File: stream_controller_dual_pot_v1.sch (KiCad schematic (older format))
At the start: 35 parts, among them Q1 Q_PMOS_GDS, Q2 Q_PMOS_GDS, SW1 SW_SPDT, U1 MCP1825S, U2 MCP2221AxSL, U3 MCP73831-2-OT, U5 ESP32_WROVER_E, U6 MIC803

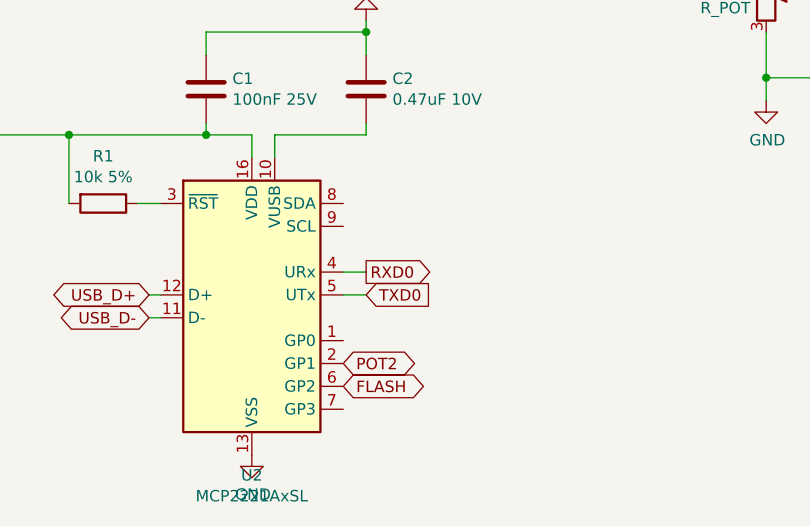
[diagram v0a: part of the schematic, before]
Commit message: bug UART corrigé
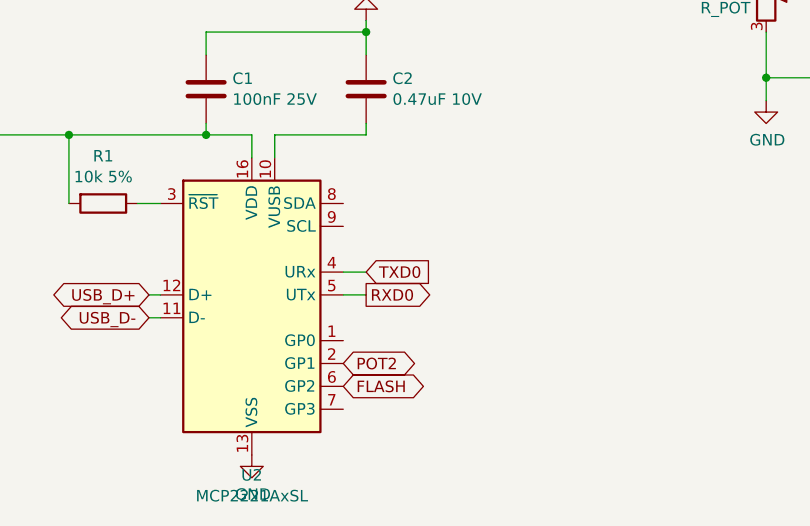
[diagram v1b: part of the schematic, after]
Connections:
- net RXD0: now also U2.5 (UTx); no longer U2.4 (URx)
- net TXD0: now also U2.4 (URx); no longer U2.5 (UTx)
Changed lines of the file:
@@
 Text GLabel 3400 4900 0    50   BiDi ~ 0
 USB_D-
-Text GLabel 4350 4700 2    50   Output ~ 0
+Text GLabel 4350 4800 2    50   Output ~ 0
 RXD0
-Text GLabel 4350 4800 2    50   Input ~ 0
+Text GLabel 4350 4700 2    50   Input ~ 0
 TXD0
 Text GLabel 9200 3900 2    50   Input ~ 0

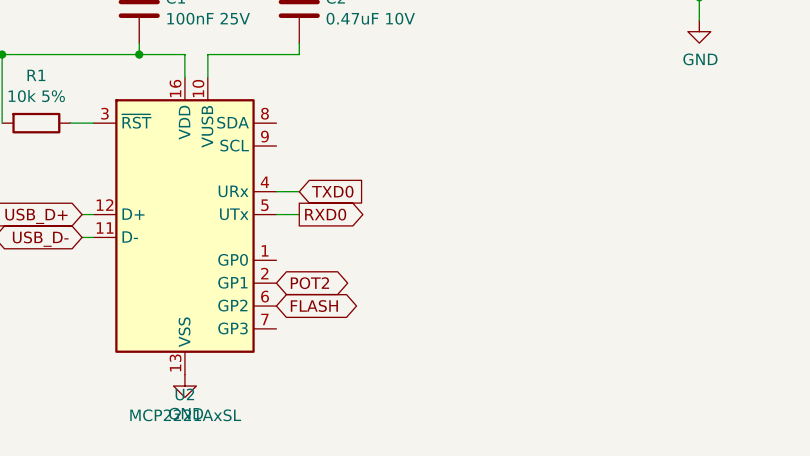
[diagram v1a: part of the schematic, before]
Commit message: Correction IO0 forcé à 1
Si IO0 n'est pas haut au démarrage, l'ESP32 se met en mode flash. Quand non-connecté par USB, IO0 doit être forcé à 1, car le contrôleur USB n'est pas alimenté.
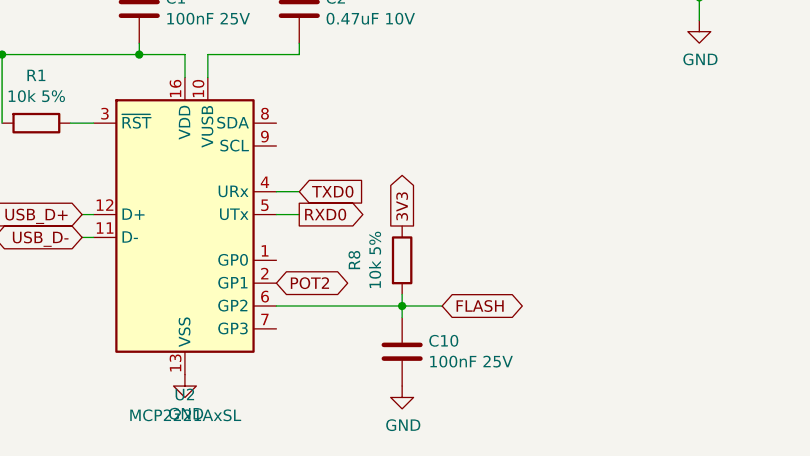
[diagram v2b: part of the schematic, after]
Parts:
- added C10: 100nF 25V, Capacitor_SMD:C_0402_1005Metric_Pad0.74x0.62mm_HandSolder, symbol Device:C
- added R8: 10k 5%, Resistor_SMD:R_0402_1005Metric_Pad0.72x0.64mm_HandSolder, symbol Device:R
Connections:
- net 3V3: now also R8.1
- net FLASH: now also C10.1, R8.2
- net GND: now also C10.2
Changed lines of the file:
@@
 EndData
 $EndBitmap
-Text GLabel 4250 5200 2    50   BiDi ~ 0
+Text GLabel 4975 5200 2    50   BiDi ~ 0
 FLASH
 Text GLabel 4250 5100 2    50   BiDi ~ 0
@@
 	3750 3300 3750 2250
 $Comp
-L power:GND #PWR?
+L power:GND #PWR0113
 U 1 1 6090601E
 P 3850 5500
-F 0 "#PWR?" H 3850 5250 50  0001 C CNN
+F 0 "#PWR0113" H 3850 5250 50  0001 C CNN
 F 1 "GND" H 3855 5327 50  0000 C CNN
 F 2 "" H 3850 5500 50  0001 C CNN
@@
 	1    0    0    -1
 $EndComp
+$Comp
+L Device:R R8
+U 1 1 609456D2
+P 4800 5000
+F 0 "R8" V 4593 5000 50  0000 C CNN
+F 1 "10k 5%" V 4684 5000 50  0000 C CNN
+F 2 "Resistor_SMD:R_0402_1005Metric_Pad0.72x0.64mm_HandSolder" V 4730 5000 50  0001 C CNN
+F 3 "~" H 4800 5000 50  0001 C CNN
+	1    4800 5000
+	1    0    0    -1
+$EndComp
+Wire Wire Line
+	4800 5150 4800 5200
+Wire Wire Line
+	4800 5200 4250 5200
+Text GLabel 4800 4850 1    50   Output ~ 0
+3V3
+$Comp
+L Device:C C10
+U 1 1 60958AC1
+P 4800 5400
+F 0 "C10" H 4915 5446 50  0000 L CNN
+F 1 "100nF 25V" H 4915 5355 50  0000 L CNN
+F 2 "Capacitor_SMD:C_0402_1005Metric_Pad0.74x0.62mm_HandSolder" H 4838 5250 50  0001 C CNN
+F 3 "~" H 4800 5400 50  0001 C CNN
+	1    4800 5400
+	1    0    0    -1
+$EndComp
+Wire Wire Line
+	4975 5200 4800 5200
+Connection ~ 4800 5200
+$Comp
+L power:GND #PWR0118
+U 1 1 60972D20
+P 4800 5550
+F 0 "#PWR0118" H 4800 5300 50  0001 C CNN
+F 1 "GND" H 4805 5377 50  0000 C CNN
+F 2 "" H 4800 5550 50  0001 C CNN
+F 3 "" H 4800 5550 50  0001 C CNN
+	1    4800 5550
+	1    0    0    -1
+$EndComp
+Wire Wire Line
+	4800 5200 4800 5250
 $EndSCHEMATC

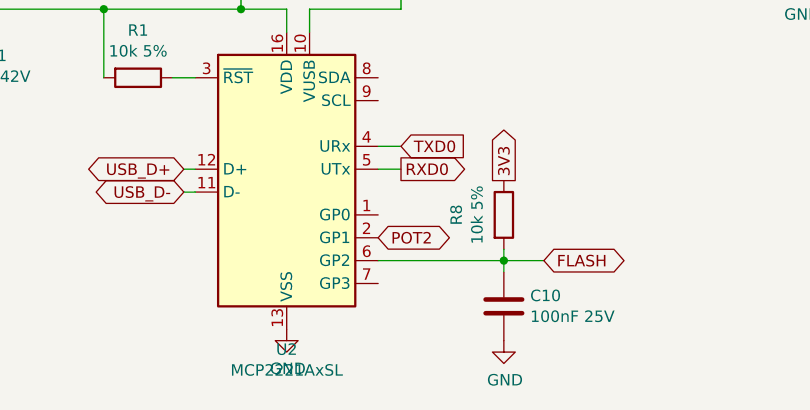
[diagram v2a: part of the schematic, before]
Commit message: Ajout contrôle pin EN par contrôleur USB
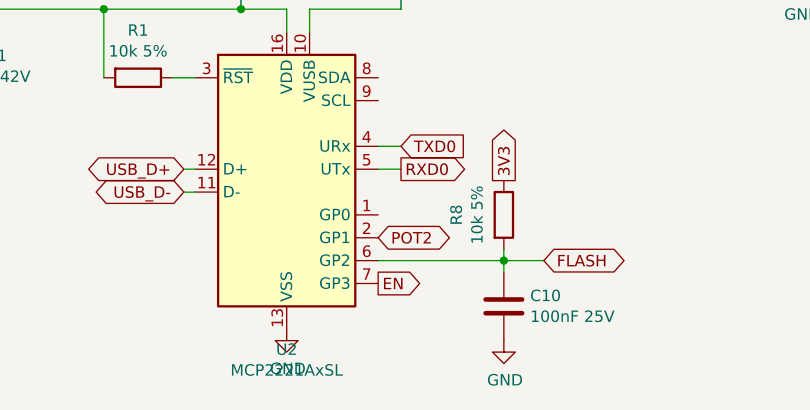
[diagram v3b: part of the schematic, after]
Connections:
- net EN: now also U2.7 (GP3)
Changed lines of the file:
@@
 Wire Wire Line
 	4800 5200 4800 5250
+Text GLabel 4250 5300 2    50   Output ~ 0
+EN
 $EndSCHEMATC

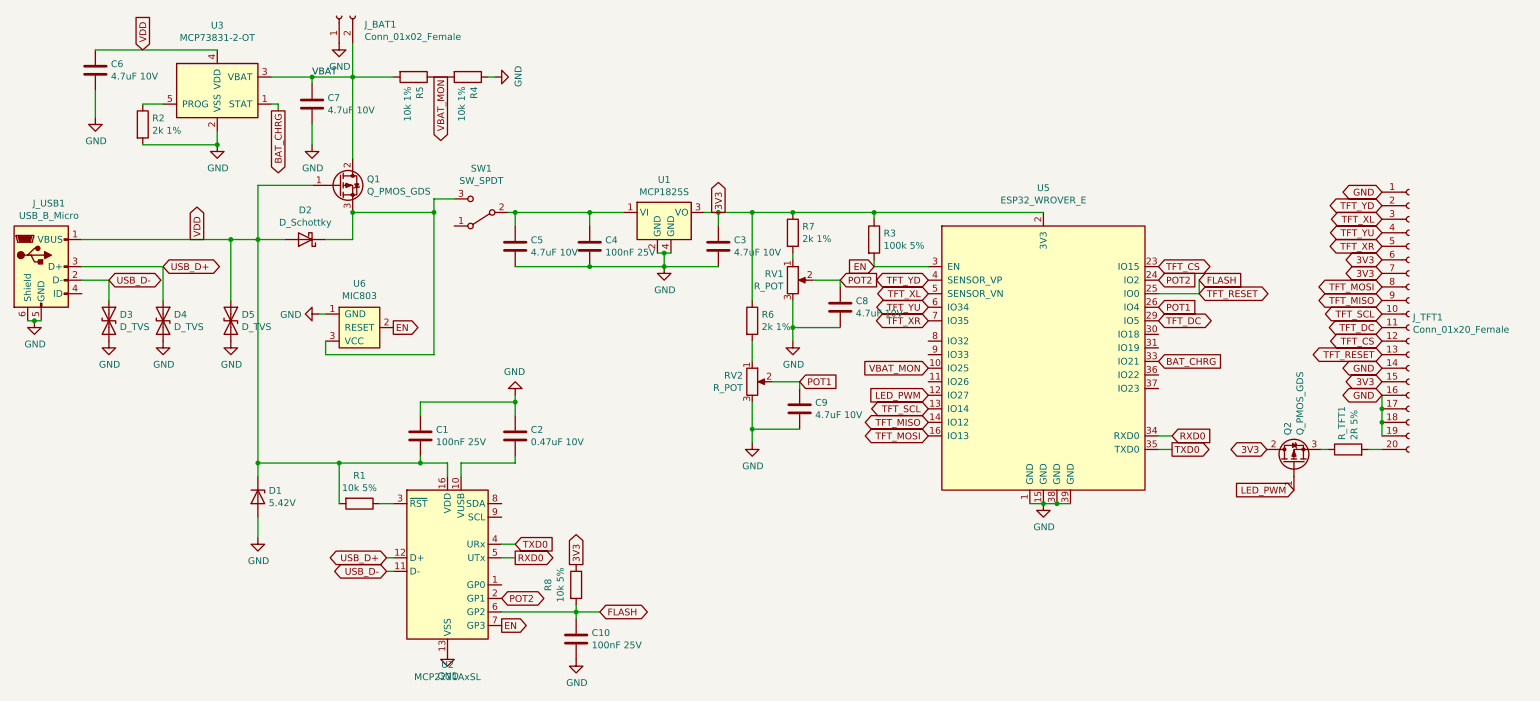
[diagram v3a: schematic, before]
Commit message: Changements divers
Modifications :
 - toutes les entrées analogiques sur ADC1, car ADC2 ne peut pas être utilisé si le WiFi est actif
 - lecture de l'écran tactile déplacée sur pattes 8, 9, 10 et 11, car les pattes 4, 5, 6 et 7 sont en lecture seule
 - changement du transistor pour le contrôle de la luminosité de l'écran
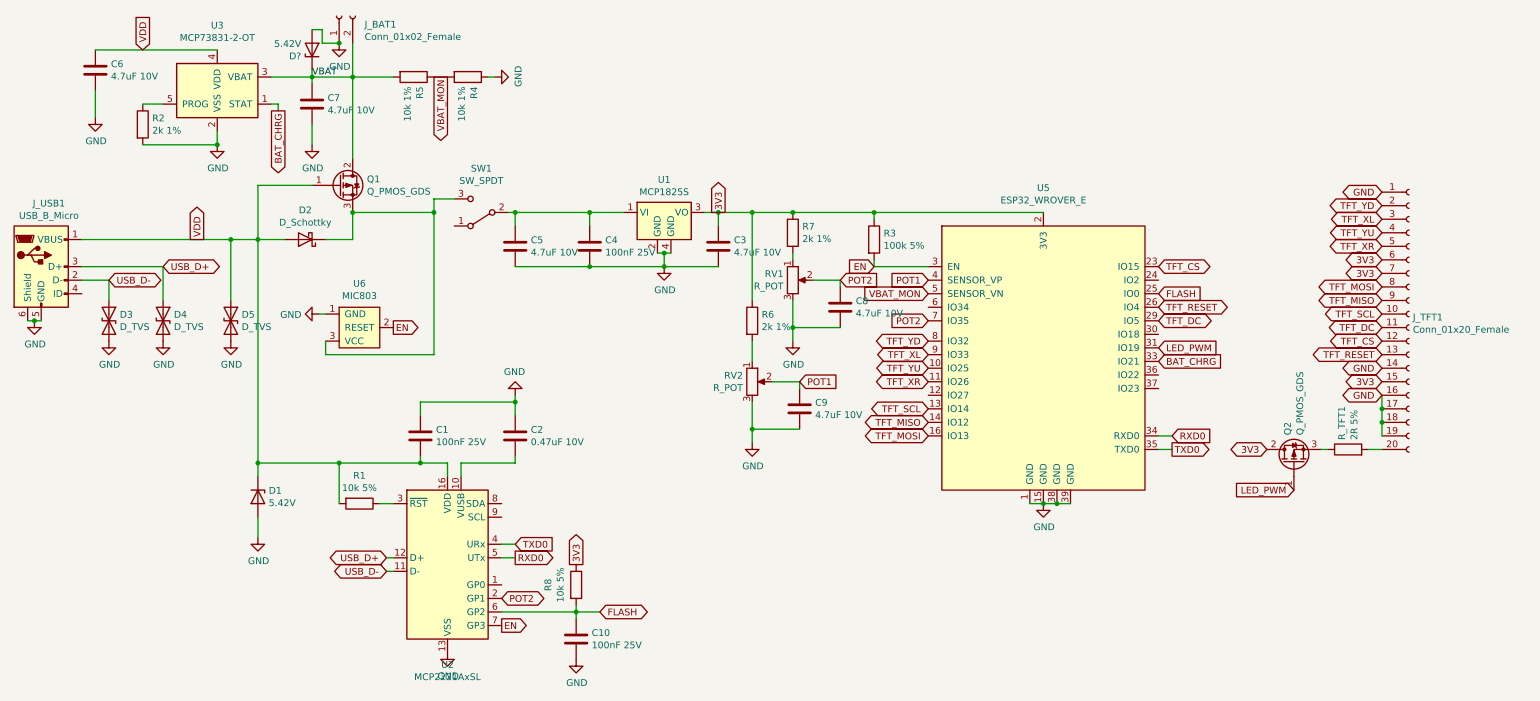
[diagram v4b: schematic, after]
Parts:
- added D?: 5.42V, Diode_SMD:D_SOD-323F, symbol Device:D_Zener
- J_BAT1: footprint Connector_PinHeader_2.54mm:PinHeader_1x02_P2.54mm_Vertical -> misc_vp:CLM-101-02-L-D
- Q2: footprint Package_DFN_QFN:Diodes_DFN1006-3 -> Package_TO_SOT_SMD:SOT-23
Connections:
- net FLASH: no longer J_TFT1.13 (Pin_13)
- net GND: now also D?.2 (A)
- net LED_PWM: now also U5.31 (IO19); no longer U5.12 (IO27)
- net POT1: now also U5.4 (SENSOR_VP); no longer U5.26 (IO4)
- net POT2: now also U5.7 (IO35); no longer U5.24 (IO2)
- net TFT_XL: now also U5.9 (IO33); no longer U5.5 (SENSOR_VN)
- net TFT_XR: now also U5.11 (IO26); no longer U5.7 (IO35)
- net TFT_YD: now also U5.8 (IO32); no longer U5.4 (SENSOR_VP)
- net TFT_YU: now also U5.10 (IO25); no longer U5.6 (IO34)
- net VBAT: now also D?.1 (K)
- net VBAT_MON: now also U5.5 (SENSOR_VN); no longer U5.10 (IO25)
- new net TFT_RESET: J_TFT1.13 (Pin_13), U5.26 (IO4)
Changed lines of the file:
@@
 F 0 "J_BAT1" V 2988 612 50  0000 R CNN
 F 1 "Conn_01x02_Female" V 2897 612 50  0000 R CNN
-F 2 "Connector_PinHeader_2.54mm:PinHeader_1x02_P2.54mm_Vertical" H 3050 800 50  0001 C CNN
+F 2 "misc_vp:CLM-101-02-L-D" H 3050 800 50  0001 C CNN
 F 3 "~" H 3050 800 50  0001 C CNN
 	1    3050 800
@@
 Wire Wire Line
 	4900 2250 5150 2250
-Text GLabel 7400 3400 0    50   Input ~ 0
+Text GLabel 7400 2850 0    50   Input ~ 0
 VBAT_MON
 Wire Wire Line
@@
 Text GLabel 9100 2650 2    50   BiDi ~ 0
 TFT_CS
-Text GLabel 9400 2850 2    50   BiDi ~ 0
+Text GLabel 9100 2950 2    50   BiDi ~ 0
 TFT_RESET
-Text GLabel 7400 2750 0    50   BiDi ~ 0
+Text GLabel 7400 3200 0    50   BiDi ~ 0
 TFT_YD
-Text GLabel 7400 2850 0    50   BiDi ~ 0
+Text GLabel 7400 3300 0    50   BiDi ~ 0
 TFT_XL
-Text GLabel 7400 2950 0    50   BiDi ~ 0
+Text GLabel 7400 3400 0    50   BiDi ~ 0
 TFT_YU
-Text GLabel 7400 3050 0    50   BiDi ~ 0
+Text GLabel 7400 3500 0    50   BiDi ~ 0
 TFT_XR
 Text GLabel 9100 3050 2    50   BiDi ~ 0
@@
 Text GLabel 6750 2750 2    50   Input ~ 0
 POT2
-Text GLabel 9100 2950 2    50   Input ~ 0
+Text GLabel 7400 2750 0    50   Input ~ 0
 POT1
 Text GLabel 9100 3350 2    50   Input ~ 0
@@
 Text Label 2850 1250 0    50   ~ 0
 VBAT
-Text GLabel 9100 2750 2    50   Input ~ 0
-POT2
-Text GLabel 9400 2750 2    50   Input ~ 0
+Text GLabel 9100 2850 2    50   Input ~ 0
 FLASH
 $Comp
@@
 Text GLabel 4250 5100 2    50   BiDi ~ 0
 POT2
-Wire Wire Line
-	9400 2750 9400 2850
 $Comp
 L Device:Q_PMOS_GDS Q2
@@
 F 0 "Q2" H 10305 4146 50  0000 L CNN
 F 1 "Q_PMOS_GDS" H 10305 4055 50  0000 L CNN
-F 2 "Package_DFN_QFN:Diodes_DFN1006-3" H 10300 4200 50  0001 C CNN
+F 2 "Package_TO_SOT_SMD:SOT-23" H 10300 4200 50  0001 C CNN
 F 3 "~" H 10100 4100 50  0001 C CNN
 	1    10100 4100
@@
 Text GLabel 10100 4300 0    50   Input ~ 0
 LED_PWM
-Text GLabel 7400 3600 0    50   Input ~ 0
+Text GLabel 9100 3250 2    50   Input ~ 0
 LED_PWM
-Wire Wire Line
-	9400 2850 9100 2850
 Text GLabel 3450 3100 2    50   Output ~ 0
 EN
@@
 Text GLabel 4250 5300 2    50   Output ~ 0
 EN
+Text GLabel 7400 3050 0    50   Input ~ 0
+POT2
+$Comp
+L Device:D_Zener D?
+U 1 1 609F24D1
+P 2850 1050
+F 0 "D?" V 2804 1130 50  0000 L CNN
+F 1 "5.42V" V 2895 1130 50  0000 L CNN
+F 2 "Diode_SMD:D_SOD-323F" H 2850 1050 50  0001 C CNN
+F 3 "~" H 2850 1050 50  0001 C CNN
+	1    2850 1050
+	0    -1   -1   0
+$EndComp
+Wire Wire Line
+	2850 1250 2850 1200
+Wire Wire Line
+	3050 1000 2925 1000
+Wire Wire Line
+	2925 1000 2925 900
+Wire Wire Line
+	2925 900  2850 900
+Connection ~ 3050 1000
 $EndSCHEMATC

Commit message: Corrections et ajouts
Corrigé : strapping pin 2 connectée au même signal FLASH que pin 0
Ajouté : I2C entre uC et contrôleur USB
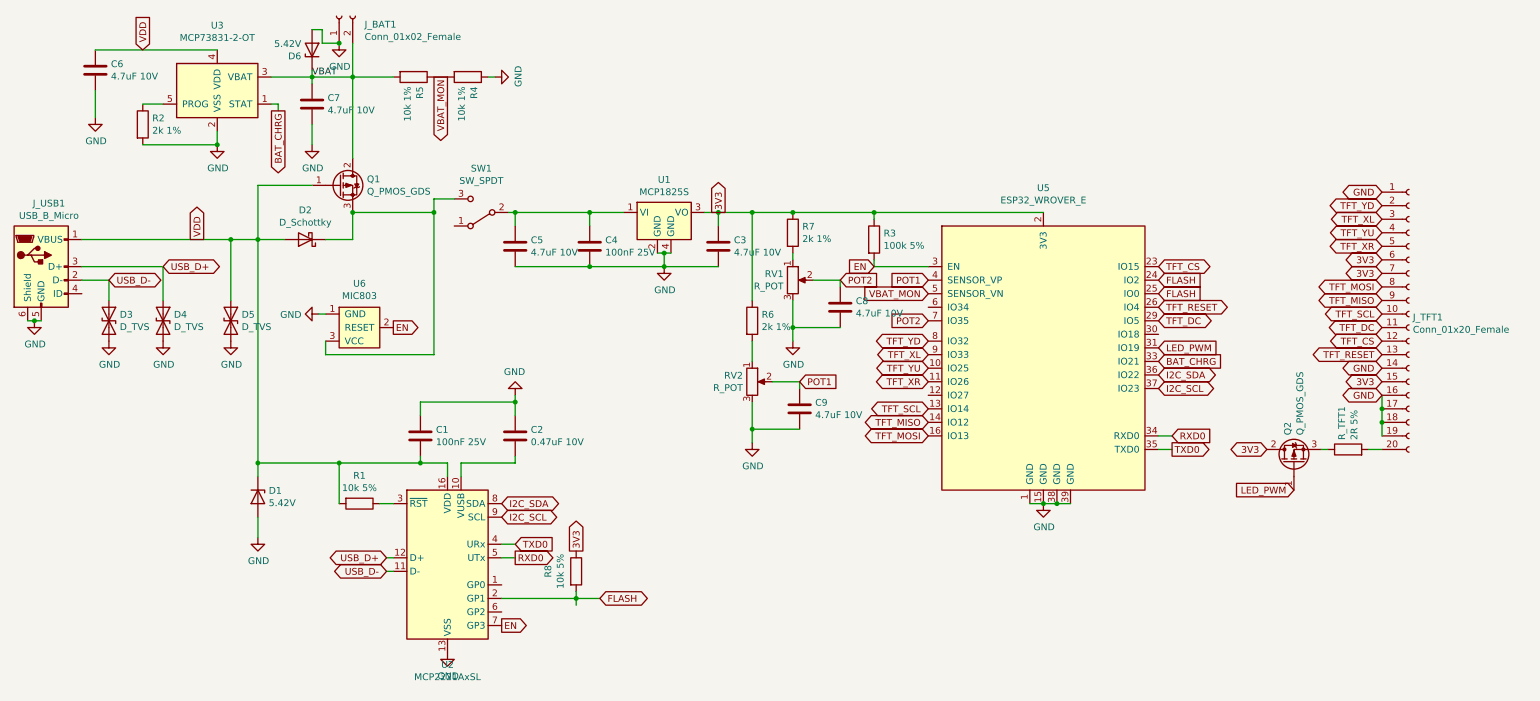
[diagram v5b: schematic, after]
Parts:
- removed C10: 100nF 25V, Capacitor_SMD:C_0402_1005Metric_Pad0.74x0.62mm_HandSolder, symbol Device:C
- J_BAT1: footprint misc_vp:CLM-101-02-L-D -> Connector_PinHeader_2.54mm:PinHeader_1x02_P2.54mm_Vertical
- gave numbers to parts that had none: 1
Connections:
- net FLASH: now also U2.2 (GP1), U5.24 (IO2); no longer U2.6 (GP2)
- net POT2: no longer U2.2 (GP1)
- net I2C_SDA: now reaches U2.8 (SDA)
- net I2C_SDA: now also U5.36 (IO22)
- net I2C_SCL: now reaches U2.9 (SCL)
- net I2C_SCL: now also U5.37 (IO23)
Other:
- moved on the sheet: R8
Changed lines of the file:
@@
 F 0 "J_BAT1" V 2988 612 50  0000 R CNN
 F 1 "Conn_01x02_Female" V 2897 612 50  0000 R CNN
-F 2 "misc_vp:CLM-101-02-L-D" H 3050 800 50  0001 C CNN
+F 2 "Connector_PinHeader_2.54mm:PinHeader_1x02_P2.54mm_Vertical" H 3050 800 50  0001 C CNN
 F 3 "~" H 3050 800 50  0001 C CNN
 	1    3050 800
@@
 EndData
 $EndBitmap
-Text GLabel 4975 5200 2    50   BiDi ~ 0
+Text GLabel 4975 5100 2    50   BiDi ~ 0
 FLASH
-Text GLabel 4250 5100 2    50   BiDi ~ 0
-POT2
 $Comp
 L Device:Q_PMOS_GDS Q2
@@
 L Device:R R8
 U 1 1 609456D2
-P 4800 5000
-F 0 "R8" V 4593 5000 50  0000 C CNN
-F 1 "10k 5%" V 4684 5000 50  0000 C CNN
-F 2 "Resistor_SMD:R_0402_1005Metric_Pad0.72x0.64mm_HandSolder" V 4730 5000 50  0001 C CNN
-F 3 "~" H 4800 5000 50  0001 C CNN
-	1    4800 5000
-	1    0    0    -1
-$EndComp
-Wire Wire Line
-	4800 5150 4800 5200
-Wire Wire Line
-	4800 5200 4250 5200
-Text GLabel 4800 4850 1    50   Output ~ 0
+P 4800 4900
+F 0 "R8" V 4593 4900 50  0000 C CNN
+F 1 "10k 5%" V 4684 4900 50  0000 C CNN
+F 2 "Resistor_SMD:R_0402_1005Metric_Pad0.72x0.64mm_HandSolder" V 4730 4900 50  0001 C CNN
+F 3 "~" H 4800 4900 50  0001 C CNN
+	1    4800 4900
+	1    0    0    -1
+$EndComp
+Wire Wire Line
+	4800 5050 4800 5100
+Wire Wire Line
+	4800 5100 4250 5100
+Text GLabel 4800 4750 1    50   Output ~ 0
 3V3
-$Comp
-L Device:C C10
-U 1 1 60958AC1
-P 4800 5400
-F 0 "C10" H 4915 5446 50  0000 L CNN
-F 1 "100nF 25V" H 4915 5355 50  0000 L CNN
-F 2 "Capacitor_SMD:C_0402_1005Metric_Pad0.74x0.62mm_HandSolder" H 4838 5250 50  0001 C CNN
-F 3 "~" H 4800 5400 50  0001 C CNN
-	1    4800 5400
-	1    0    0    -1
-$EndComp
-Wire Wire Line
-	4975 5200 4800 5200
-Connection ~ 4800 5200
-$Comp
-L power:GND #PWR0118
-U 1 1 60972D20
-P 4800 5550
-F 0 "#PWR0118" H 4800 5300 50  0001 C CNN
-F 1 "GND" H 4805 5377 50  0000 C CNN
-F 2 "" H 4800 5550 50  0001 C CNN
-F 3 "" H 4800 5550 50  0001 C CNN
-	1    4800 5550
-	1    0    0    -1
-$EndComp
-Wire Wire Line
-	4800 5200 4800 5250
+Wire Wire Line
+	4975 5100 4800 5100
+Connection ~ 4800 5100
+Wire Wire Line
+	4800 5100 4800 5150
 Text GLabel 4250 5300 2    50   Output ~ 0
 EN
@@
 POT2
 $Comp
-L Device:D_Zener D?
+L Device:D_Zener D6
 U 1 1 609F24D1
 P 2850 1050
-F 0 "D?" V 2804 1130 50  0000 L CNN
+F 0 "D6" V 2804 1130 50  0000 L CNN
 F 1 "5.42V" V 2895 1130 50  0000 L CNN
 F 2 "Diode_SMD:D_SOD-323F" H 2850 1050 50  0001 C CNN
@@
 	2925 900  2850 900
 Connection ~ 3050 1000
+Text GLabel 9100 2750 2    50   Input ~ 0
+FLASH
+Text GLabel 4250 4400 2    50   BiDi ~ 0
+I2C_SDA
+Text GLabel 4250 4500 2    50   BiDi ~ 0
+I2C_SCL
+Text GLabel 9100 3450 2    50   BiDi ~ 0
+I2C_SDA
+Text GLabel 9100 3550 2    50   BiDi ~ 0
+I2C_SCL
 $EndSCHEMATC
